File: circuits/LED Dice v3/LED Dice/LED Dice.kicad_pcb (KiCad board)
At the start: 4 copper layers, 50.8 x 25.4 mm, 48 parts, among them J1 KH-TYPE-C-16P, J3 Conn_01x02_Pin, J4 Conn_01x03_Pin, U1 STM32F042F6Px, U2 TTP223-BA6, U3 TP4057, U4 LTST-C195KGJRKT, U5 TLV74333PDBVR, U6 MT3608

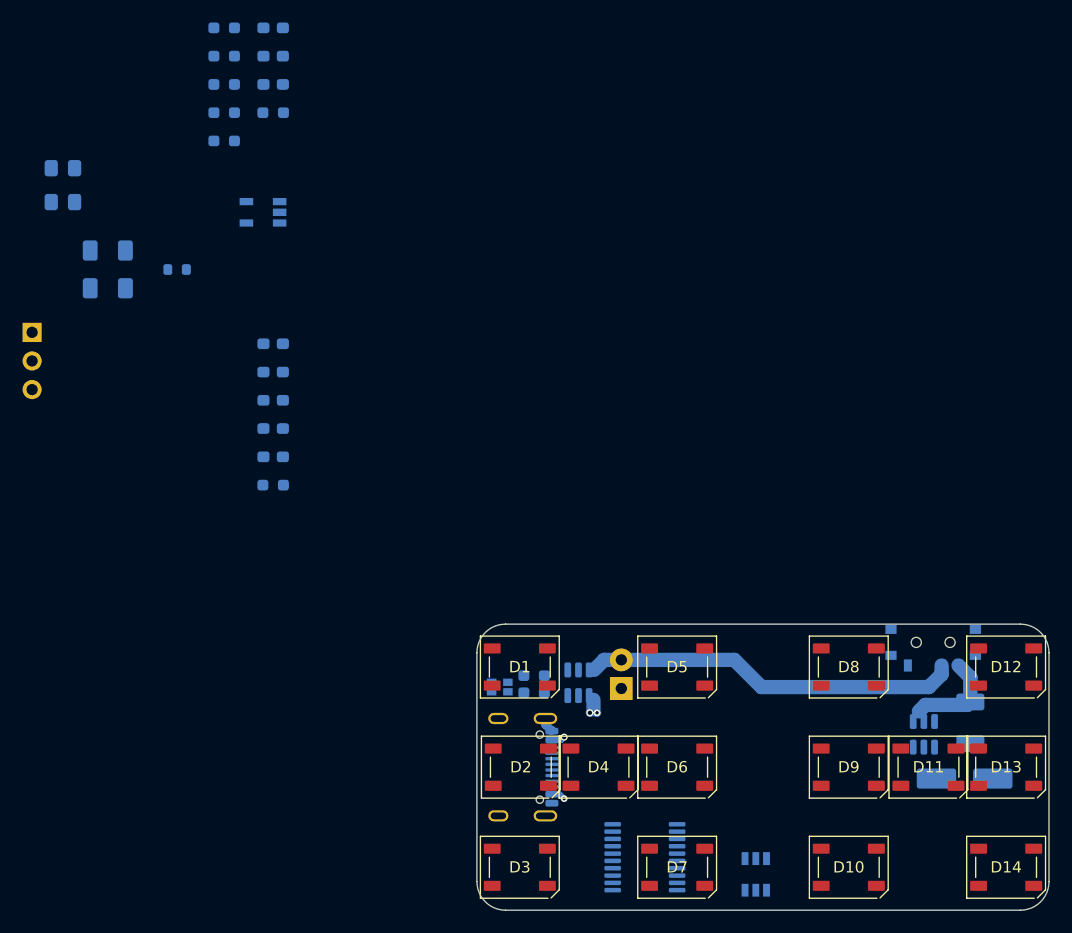
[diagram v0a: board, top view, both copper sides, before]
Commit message: layout complete, some DRC violations are present
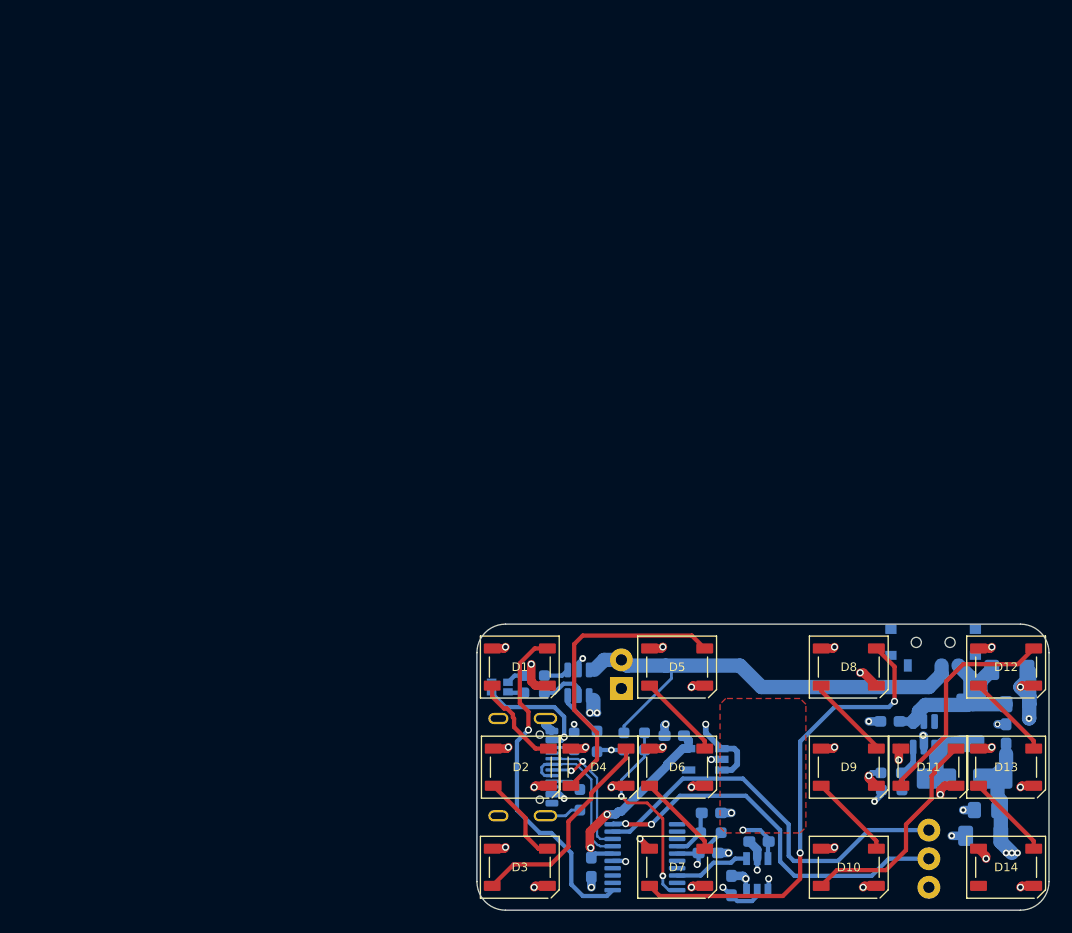
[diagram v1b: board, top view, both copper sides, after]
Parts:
- moved C11 98.2 mm to (172.2, 92.7)
- moved C7 97.2 mm to (175.0, 83.3), turned to 0 degrees
- moved C12 91.7 mm to (172.0, 95.0)
- moved J4 91.1 mm to (167.1, 94.5)
- moved C8 88.3 mm to (174.3, 80.3), turned to 0 degrees
- moved R7 88.1 mm to (163.8, 90.9), turned to 0 degrees
- moved C10 87.0 mm to (174.0, 86.0), turned to 90 degrees
- moved R8 85.1 mm to (163.8, 89.4)
- moved C9 80.6 mm to (163.7, 84.8)
- moved C6 72.2 mm to (144.5, 86.1)
- moved R6 71.5 mm to (137.7, 86.6), turned to -90 degrees
- moved R2 66.8 mm to (136.1, 91.8), turned to 90 degrees
- moved R9 66.0 mm to (141.0, 85.9), turned to 0 degrees
- moved R10 65.2 mm to (141.0, 87.4)
- moved U5 62.5 mm to (147.3, 88.2)
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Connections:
- U5 pad 1: /Power and Comms/VBatt+ -> +5V
- U5 pad 3: /Power and Comms/VBatt+ -> +5V
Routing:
- net GND: track 1.33 -> 56.1 mm, vias 0 -> 32
- net /LED Matrix 2/Din: track 0.00 -> 41.8 mm, vias 0 -> 2
- net /Microcontroller/SWDIO: track 0.00 -> 35.8 mm
- net +5V: track 0.00 -> 35.3 mm, vias 0 -> 19
- net /Microcontroller/SWCLK: track 0.00 -> 34.4 mm, vias 0 -> 2
- net /LED matrix 1/Din: track 0.00 -> 30.3 mm, vias 0 -> 1
- net +3.3V: track 0.00 -> 27.6 mm, vias 0 -> 4
- net Net-(D4-DOUT): track 0.00 -> 26.8 mm
- net Net-(D11-DOUT): track 0.00 -> 19.9 mm
- net Net-(D10-DOUT): track 0.00 -> 19.7 mm
- net Net-(D3-DOUT): track 0.00 -> 19.0 mm
- net /Microcontroller/Vsample: track 0.00 -> 18.3 mm, vias 0 -> 2
- net /Microcontroller/USB D+: track 0.00 -> 14.6 mm, vias 0 -> 2
- net /Microcontroller/USB D-: track 0.00 -> 14.0 mm
- net /Power and Comms/Vbus: track 3.73 -> 13.8 mm
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- added copper zone on In2.Cu, net +3.3V
- added copper zone on F.Cu, net /Microcontroller/touchIn

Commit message: All meaningful DRC resolved
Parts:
- moved C9 0.46 mm to (163.2, 84.8)
- moved R1 0.32 mm to (135.8, 86.3)
- moved C7 0.13 mm to (175.1, 83.3)
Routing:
- net +5V: track 35.3 -> 40.1 mm
- net /Power and Comms/VBatt+: track 17.8 -> 18.5 mm
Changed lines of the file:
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@@
 	(footprint "Resistor_SMD:R_0603_1608Metric"
 		(layer "B.Cu")
-		(at 135.636 86.614 -90)
+		(at 135.763 86.325 -90)
 		(descr "Resistor SMD 0603 (1608 Metric), square (rectangular) end terminal, IPC-7351 nominal, (Body size source: IPC-SM-782 page 72, https://www.pcb-3d.com/wordpress/wp-content/uploads/ipc-sm-782a_amendment_1_and_2.pdf)")
 		(tags "resistor")
@@
 	(footprint "Capacitor_SMD:C_0805_2012Metric_Pad1.18x1.45mm_HandSolder"
 		(layer "B.Cu")
-		(at 175.006 83.312)
+		(at 175.133 83.312)
 		(descr "Capacitor SMD 0805 (2012 Metric), square (rectangular) end terminal, IPC-7351 nominal with elongated pad for handsoldering. (Body size source: IPC-SM-782 page 76, https://www.pcb-3d.com/wordpress/wp-content/uploads/ipc-sm-782a_amendment_1_and_2.pdf, https://docs.google.com/spreadsheets/d/1BsfQQcO9C6DZCsRaXUlFlo91Tg2WpOkGARC1WS5S8t0/edit?usp=sharing)")
 		(tags "capacitor handsolder")
@@
 	(footprint "Capacitor_SMD:C_0603_1608Metric_Pad1.08x0.95mm_HandSolder"
 		(layer "B.Cu")
-		(at 163.6765 84.836 180)
+		(at 163.2215 84.836 180)
 		(descr "Capacitor SMD 0603 (1608 Metric), square (rectangular) end terminal, IPC-7351 nominal with elongated pad for handsoldering. (Body size source: IPC-SM-782 page 76, https://www.pcb-3d.com/wordpress/wp-content/uploads/ipc-sm-782a_amendment_1_and_2.pdf)")
 		(tags "capacitor handsolder")
@@
 	)
 	(segment
-		(start 136.524 87.25)
-		(end 136.652 87.122)
+		(start 129.412 96.14)
+		(end 129.54 96.012)
 		(width 0.762)
 		(layer "F.Cu")
@@
 	)
 	(segment
-		(start 129.412 96.14)
-		(end 129.54 96.012)
+		(start 128.36 78.36)
+		(end 129.412 78.36)
 		(width 0.762)
 		(layer "F.Cu")
@@
 	)
 	(segment
-		(start 128.36 78.36)
-		(end 129.412 78.36)
+		(start 129.8702 88.519)
+		(end 134.203 88.519)
 		(width 0.762)
 		(layer "F.Cu")
@@
 	)
 	(segment
+		(start 134.203 88.519)
+		(end 135.472 87.25)
+		(width 0.762)
+		(layer "F.Cu")
+		(net "+5V")
+	)
+	(segment
 		(start 143.382 78.36)
 		(end 142.33 78.36)
@@
 	)
 	(segment
-		(start 135.472 87.25)
-		(end 136.524 87.25)
-		(width 0.762)
-		(layer "F.Cu")
-		(net "+5V")
-	)
-	(segment
 		(start 158.622 96.14)
 		(end 158.75 96.012)
@@
 	)
 	(via
-		(at 136.652 87.122)
+		(at 129.8702 88.519)
 		(size 0.635)
 		(drill 0.381)
@@
 	)
 	(via
-		(at 135.636 85.09)
+		(at 135.509 84.836)
 		(size 0.6)
 		(drill 0.3)
@@
 	)
 	(via
-		(at 161.798 84.836)
+		(at 161.544 84.836)
 		(size 0.6)
 		(drill 0.3)
@@
 	)
 	(segment
+		(start 133.66 92.1)
+		(end 133.66 92.645)
+		(width 0.508)
+		(layer "B.Cu")
+		(net "GND")
+	)
+	(segment
+		(start 133.66 92.645)
+		(end 133.085 93.22)
+		(width 1.27)
+		(layer "B.Cu")
+		(net "GND")
+	)
+	(segment
 		(start 135.382 92.71)
 		(end 134.872 93.22)
@@
 	)
 	(segment
+		(start 162.0785 84.836)
+		(end 161.544 84.836)
+		(width 0.762)
+		(layer "B.Cu")
+		(net "GND")
+	)
+	(segment
 		(start 149.606 98.552)
 		(end 150.622 98.552)
@@
 	)
 	(segment
-		(start 135.636 85.09)
-		(end 135.636 85.789)
+		(start 135.509 84.836)
+		(end 135.509 85.154)
 		(width 0.254)
 		(layer "B.Cu")
@@
 	)
 	(segment
-		(start 162.814 84.836)
-		(end 161.798 84.836)
-		(width 0.762)
-		(layer "B.Cu")
-		(net "GND")
-	)
-	(segment
 		(start 147.824041 88.204002)
 		(end 147.810543 88.2175)
@@
 	)
 	(segment
+		(start 129.54 83.566)
+		(end 128.307 82.333)
+		(width 0.381)
+		(layer "B.Cu")
+		(net "/Power and Comms/Vbus")
+	)
+	(segment
 		(start 134.353 91.3)
 		(end 134.747 91.694)
@@
 	(segment
 		(start 133.880357 83.566)
-		(end 134.747 84.432643)
+		(end 129.54 83.566)
 		(width 0.381)
 		(layer "B.Cu")
@@
 	)
 	(segment
-		(start 128.307 82.213)
-		(end 128.307 82.333)
+		(start 134.747 86.233)
+		(end 134.747 84.432643)
 		(width 0.381)
 		(layer "B.Cu")
@@
 	)
 	(segment
-		(start 128.307 82.333)
-		(end 129.54 83.566)
+		(start 134.747 84.432643)
+		(end 133.880357 83.566)
 		(width 0.381)
 		(layer "B.Cu")
@@
 	)
 	(segment
-		(start 128.307 81.363)
-		(end 128.307 82.213)
-		(width 0.381)
+		(start 134.747 86.233)
+		(end 134.48 86.5)
+		(width 0.508)
 		(layer "B.Cu")
 		(net "/Power and Comms/Vbus")
 	)
 	(segment
-		(start 134.48 86.5)
-		(end 134.747 86.233)
-		(width 0.508)
+		(start 128.307 81.363)
+		(end 128.307 82.213)
+		(width 0.381)
 		(layer "B.Cu")
 		(net "/Power and Comms/Vbus")
 	)
 	(segment
-		(start 133.66 86.5)
-		(end 134.48 86.5)
-		(width 0.508)
+		(start 128.307 82.333)
+		(end 128.307 82.213)
+		(width 0.381)
 		(layer "B.Cu")
 		(net "/Power and Comms/Vbus")
@@
 	)
 	(segment
-		(start 134.747 84.432643)
-		(end 134.747 86.233)
-		(width 0.381)
-		(layer "B.Cu")
-		(net "/Power and Comms/Vbus")
-	)
-	(segment
-		(start 129.54 83.566)
-		(end 133.880357 83.566)
-		(width 0.381)
+		(start 134.48 86.5)
+		(end 133.66 86.5)
+		(width 0.508)
 		(layer "B.Cu")
 		(net "/Power and Comms/Vbus")
@@
 	(segment
 		(start 135.347 87.15)
-		(end 135.636 87.439)
+		(end 135.693 86.804)
+		(width 0.254)
+		(layer "B.Cu")
+		(net "Net-(J1-CC2)")
+	)
+	(segment
+		(start 135.693 86.804)
+		(end 135.763 86.804)
 		(width 0.254)
 		(layer "B.Cu")
@@
 	(segment
 		(start 165.74 84.847)
-		(end 164.55 84.847)
+		(end 163.8145 84.847)
 		(width 0.762)
 		(layer "B.Cu")
@@
 	)
 	(segment
+		(start 163.8145 84.847)
+		(end 163.8035 84.836)
+		(width 0.762)
+		(layer "B.Cu")
+		(net "/Power and Comms/VBatt+")
+	)
+	(segment
 		(start 166.8183 83.3717)
 		(end 166.243 83.947)
@@
 	)
 	(segment
-		(start 164.55 84.847)
-		(end 164.539 84.836)
-		(width 0.762)
-		(layer "B.Cu")
-		(net "/Power and Comms/VBatt+")
-	)
-	(segment
 		(start 170.815 80.924)
 		(end 169.763 79.872)
@@
 			(pts
 				(xy 136.906 94.996) (xy 136.144 95.758) (xy 136.144 97.282) (xy 139.192 100.33) (xy 148.9445 100.33)
-				(xy 149.86 99.4145) (xy 149.86 96.266) (xy 149.352 95.758) (xy 146.05 95.758) (xy 144.526 97.282)
+				(xy 149.86 99.4145) (xy 149.86 97.917) (xy 148.717 96.774) (xy 145.02092 96.784311) (xy 144.526 97.282)
 				(xy 140.97 97.282) (xy 138.684 94.996)
 			)

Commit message: gerbers and BOM generated
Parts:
- added G***: LOGO, LOGO, B.Cu at (155.7, 83.6)
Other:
- board text added: "+ -"
- board text added: "23 Jun 2026"
- board text added: "DIO CLK GND"
- board text added: "LED Dice v3"
